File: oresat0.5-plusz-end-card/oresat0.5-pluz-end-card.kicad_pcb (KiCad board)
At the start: 4 copper layers, 99.8 x 94.6 mm, 44 parts, among them J1 J-SAMTEC-TFM-120-01-L-D-RA, J2 Harwin M55-7101242R, J3 Harwin M55-7101242R, J4 Harwin M55-7101242R, J5 Harwin M55-7101242R, J6 Conn_Coaxial

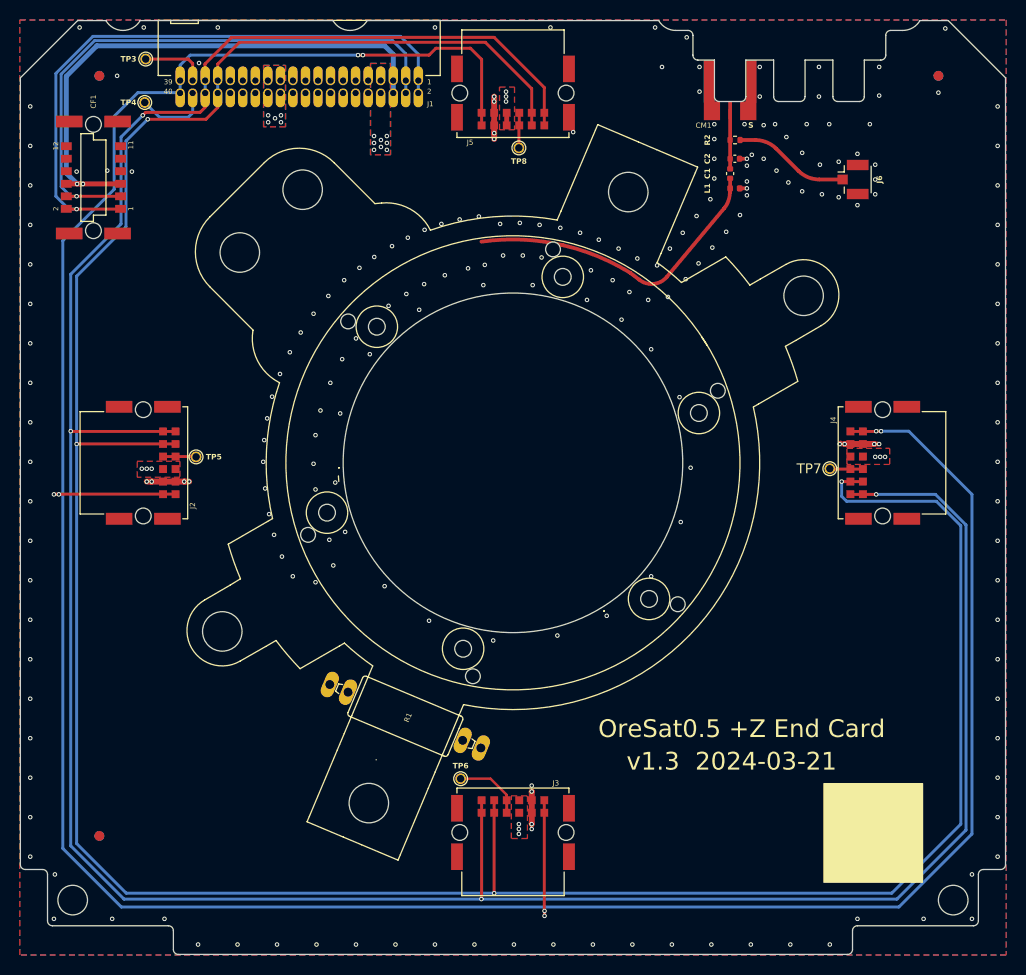
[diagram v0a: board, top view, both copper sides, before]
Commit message: Updated date, and unecessary and obsessive widening and smoothing of planes.
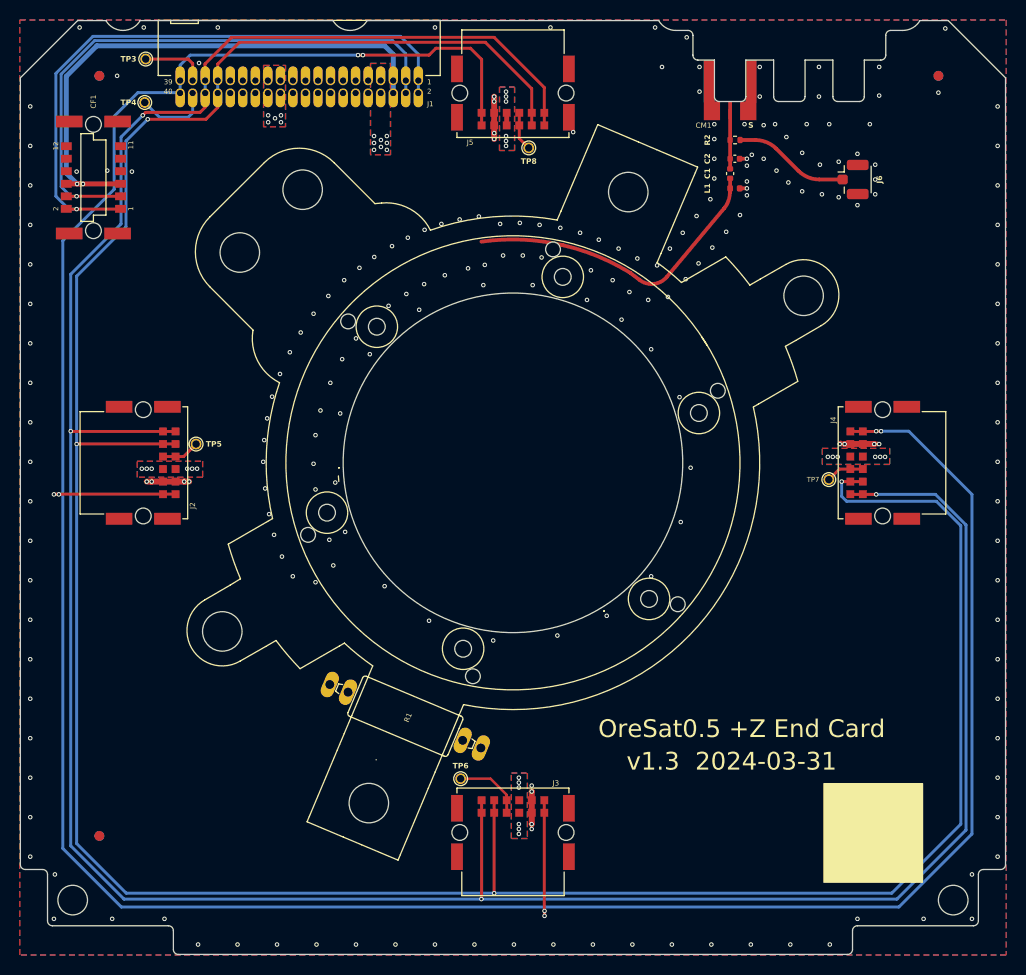
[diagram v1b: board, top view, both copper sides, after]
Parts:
- HW10, HW11, HW12, HW13, HW14, HW9: value Val** -> M2-Press-Fit-Nut
- moved TP5 1.30 mm to (116.4, 100.6)
- moved TP7 1.11 mm to (180.5, 104.2)
- moved TP8 1.00 mm to (150.1, 70.6)
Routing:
- net /-Y_AUX: track 3.66 -> 4.30 mm
- net /+Y_AUX: track 3.37 -> 3.89 mm
- net VBUS: vias 17 -> 29
- removed copper zone on In1.Cu, net /HELICAL-DEPLOY
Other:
- board text added: "v1.3 2024-03-31"
- board text removed: "v1.3 2024-03-21"

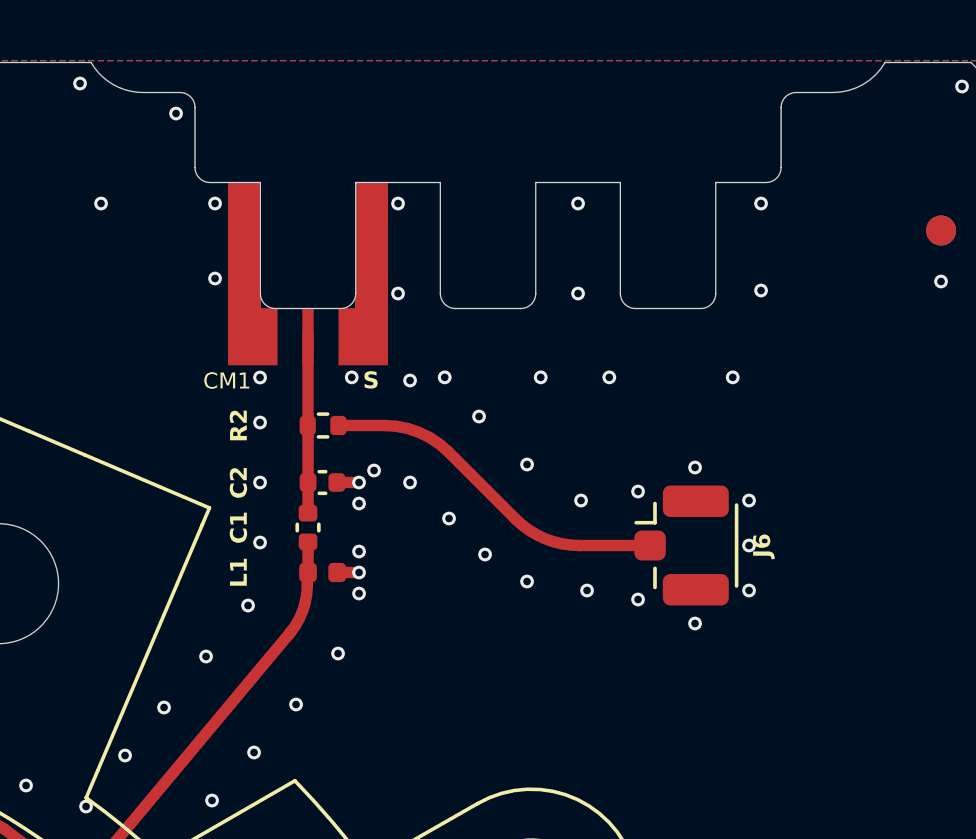
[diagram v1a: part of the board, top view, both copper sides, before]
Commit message: Updated helical matching network components and values
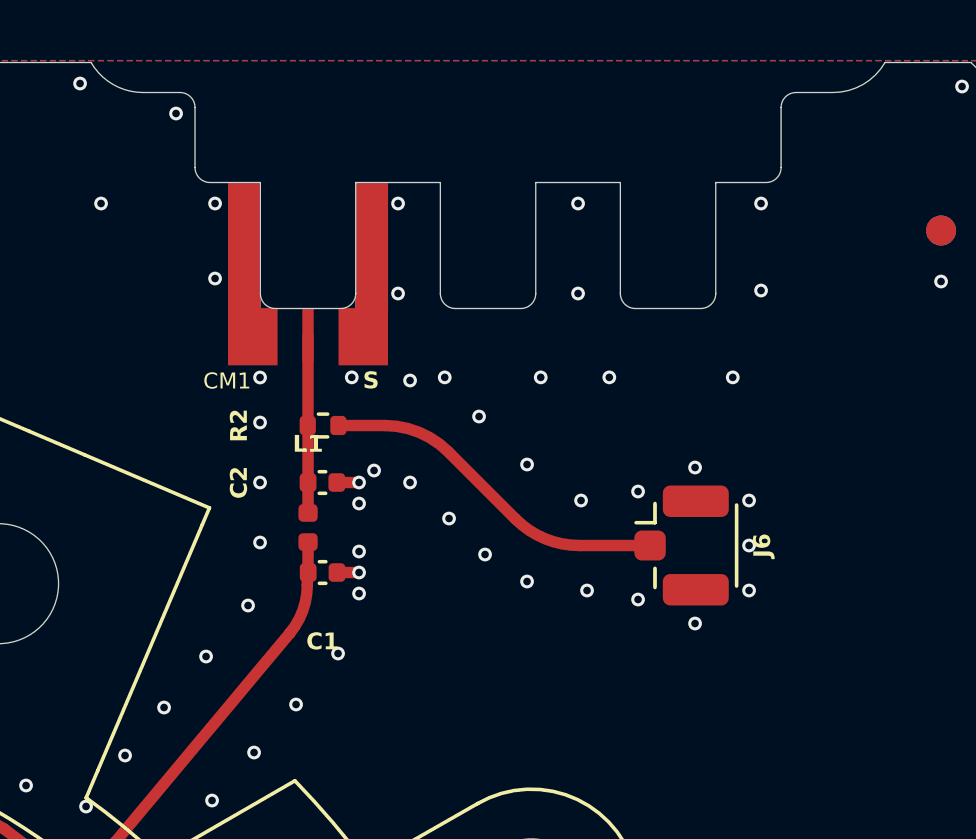
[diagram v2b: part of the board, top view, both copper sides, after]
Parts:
- C1: value C -> 1.0 pF
- C2: value NP -> 0.9 pF
- L1: value L -> 4.2 pF
- moved C1 1.58 mm to (171.0, 74.7), turned to 0 degrees
- moved L1 1.58 mm to (170.5, 73.2), turned to -90 degrees
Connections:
- C1 pad 1: /S_BAND -> /S_BAND_FEED
- C1 pad 2: /S_BAND_FEED -> GND
- L1 pad 1: /S_BAND_FEED -> /S_BAND
- L1 pad 2: GND -> /S_BAND_FEED
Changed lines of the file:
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@@
 			)
 		)
-		(property "Value" "NP"
+		(property "Value" "0.9 pF"
 			(at 0 1.16 0)
 			(layer "F.Fab")
@@
 		(fp_arc
 			(start 17.73205 -43.8)
-			(mid 18.085606 -43.653542)
+			(mid 18.085571 -43.653536)
 			(end 18.23205 -43.3)
 			(stroke
@@
 		(fp_arc
 			(start 18.73205 -40.8)
-			(mid 18.378494 -40.946458)
+			(mid 18.378529 -40.946464)
 			(end 18.23205 -41.3)
 			(stroke
@@
 		(fp_arc
 			(start 37.76795 -43.3)
-			(mid 37.9144 -43.653536)
+			(mid 37.914394 -43.653571)
 			(end 38.26795 -43.8)
 			(stroke
@@
 		(fp_arc
 			(start 37.76795 -41.3)
-			(mid 37.6215 -40.946464)
+			(mid 37.621506 -40.946429)
 			(end 37.26795 -40.8)
 			(stroke
@@
 		(fp_arc
 			(start 17.73205 -43.8)
-			(mid 18.085606 -43.653542)
+			(mid 18.085571 -43.653536)
 			(end 18.23205 -43.3)
 			(stroke
@@
 		(fp_arc
 			(start 18.73205 -40.8)
-			(mid 18.378494 -40.946458)
+			(mid 18.378529 -40.946464)
 			(end 18.23205 -41.3)
 			(stroke
@@
 		(fp_arc
 			(start 37.76795 -43.3)
-			(mid 37.9144 -43.653536)
+			(mid 37.914394 -43.653571)
 			(end 38.26795 -43.8)
 			(stroke
@@
 		(fp_arc
 			(start 37.76795 -41.3)
-			(mid 37.6215 -40.946464)
+			(mid 37.621506 -40.946429)
 			(end 37.26795 -40.8)
 			(stroke
@@
 	(footprint "Inductor_SMD:L_0402_1005Metric"
 		(layer "F.Cu")
-		(at 170.985 74.7)
+		(at 170.5 73.2 -90)
 		(descr "Inductor SMD 0402 (1005 Metric), square (rectangular) end terminal, IPC_7351 nominal, (Body size source: http://www.tortai-tech.com/upload/download/2011102023233369053.pdf), generated with kicad-footprint-generator")
 		(tags "inductor")
 		(property "Reference" "L1"
-			(at -2.785 0 90)
+			(at -2.785 0 180)
 			(layer "F.SilkS")
 			(effects
@@
 			)
 		)
-		(property "Value" "L"
-			(at -5.08 -0.508 0)
+		(property "Value" "4.2 pF"
+			(at -5.08 -0.508 90)
 			(layer "F.Fab")
 			(hide yes)
@@
 		)
 		(property "Footprint" "Inductor_SMD:L_0402_1005Metric"
-			(at 0 0 0)
+			(at 0 0 -90)
 			(unlocked yes)
 			(layer "F.Fab")
@@
 		)
 		(property "Datasheet" ""
-			(at 0 0 0)
+			(at 0 0 -90)
 			(unlocked yes)
 			(layer "F.Fab")
@@
 		)
 		(property "Description" ""
-			(at 0 0 0)
+			(at 0 0 -90)
 			(unlocked yes)
 			(layer "F.Fab")
@@
 		(attr smd)
 		(fp_line
-			(start -0.93 -0.47)
-			(end 0.93 -0.47)
+			(start -0.93 0.47)
+			(end -0.93 -0.47)
 			(stroke
 				(width 0.05)
@@
 		)
 		(fp_line
-			(start -0.93 0.47)
-			(end -0.93 -0.47)
+			(start 0.93 0.47)
+			(end -0.93 0.47)
 			(stroke
 				(width 0.05)
@@
 		)
 		(fp_line
-			(start 0.93 -0.47)
-			(end 0.93 0.47)
+			(start -0.93 -0.47)
+			(end 0.93 -0.47)
 			(stroke
 				(width 0.05)
@@
 		)
 		(fp_line
-			(start 0.93 0.47)
-			(end -0.93 0.47)
+			(start 0.93 -0.47)
+			(end 0.93 0.47)
 			(stroke
 				(width 0.05)
@@
 		)
 		(fp_line
-			(start -0.5 -0.25)
-			(end 0.5 -0.25)
+			(start -0.5 0.25)
+			(end -0.5 -0.25)
 			(stroke
 				(width 0.1)
@@
 		)
 		(fp_line
-			(start -0.5 0.25)
-			(end -0.5 -0.25)
+			(start 0.5 0.25)
+			(end -0.5 0.25)
 			(stroke
 				(width 0.1)
@@
 		)
 		(fp_line
-			(start 0.5 -0.25)
-			(end 0.5 0.25)
+			(start -0.5 -0.25)
+			(end 0.5 -0.25)
 			(stroke
 				(width 0.1)
@@
 		)
 		(fp_line
-			(start 0.5 0.25)
-			(end -0.5 0.25)
+			(start 0.5 -0.25)
+			(end 0.5 0.25)
 			(stroke
 				(width 0.1)
@@
 		)
 		(fp_text user "${REFERENCE}"
-			(at 0 0 0)
+			(at 0 0 90)
 			(layer "F.Fab")
 			(effects
@@
 		)
 		(pad "1" smd roundrect
-			(at -0.485 0)
+			(at -0.485 0 270)
 			(size 0.59 0.64)
 			(layers "F.Cu" "F.Paste" "F.Mask")
 			(roundrect_rratio 0.25)
-			(net 38 "/S_BAND_FEED")
+			(net 16 "/S_BAND")
 			(pinfunction "1")
 			(pintype "passive")
 		)
 		(pad "2" smd roundrect
-			(at 0.485 0)
+			(at 0.485 0 270)
 			(size 0.59 0.64)
 			(layers "F.Cu" "F.Paste" "F.Mask")
 			(roundrect_rratio 0.25)
-			(net 2 "GND")
+			(net 38 "/S_BAND_FEED")
 			(pinfunction "2")
 			(pintype "passive")
@@
 	(footprint "Capacitor_SMD:C_0402_1005Metric"
 		(layer "F.Cu")
-		(at 170.5 73.2 -90)
+		(at 170.985 74.7)
 		(descr "Capacitor SMD 0402 (1005 Metric), square (rectangular) end terminal, IPC_7351 nominal, (Body size source: IPC-SM-782 page 76, https://www.pcb-3d.com/wordpress/wp-content/uploads/ipc-sm-782a_amendment_1_and_2.pdf), generated with kicad-footprint-generator")
 		(tags "capacitor")
 		(property "Reference" "C1"
-			(at 0 2.3 90)
+			(at 0 2.3 360)
 			(layer "F.SilkS")
 			(effects
@@
 			)
 		)
-		(property "Value" "C"
-			(at -2.286 2.032 90)
+		(property "Value" "1.0 pF"
+			(at -2.286 2.032 360)
 			(layer "F.Fab")
 			(hide yes)
@@
 		)
 		(property "Footprint" "Capacitor_SMD:C_0402_1005Metric"
-			(at 0 0 -90)
+			(at 0 0 0)
 			(unlocked yes)
 			(layer "F.Fab")
@@
 		)
 		(property "Datasheet" ""
-			(at 0 0 -90)
+			(at 0 0 0)
 			(unlocked yes)
 			(layer "F.Fab")
@@
 		)
 		(property "Description" ""
-			(at 0 0 -90)
+			(at 0 0 0)
 			(unlocked yes)
 			(layer "F.Fab")
@@
 		(attr smd)
 		(fp_line
-			(start -0.107836 0.36)
-			(end 0.107836 0.36)
+			(start -0.107836 -0.36)
+			(end 0.107836 -0.36)
 			(stroke
 				(width 0.12)
@@
 		)
 		(fp_line
-			(start -0.107836 -0.36)
-			(end 0.107836 -0.36)
+			(start -0.107836 0.36)
+			(end 0.107836 0.36)
 			(stroke
 				(width 0.12)
@@
 		)
 		(fp_line
-			(start -0.91 0.46)
-			(end -0.91 -0.46)
+			(start -0.91 -0.46)
+			(end 0.91 -0.46)
 			(stroke
 				(width 0.05)
@@
 		)
 		(fp_line
-			(start 0.91 0.46)
-			(end -0.91 0.46)
+			(start -0.91 0.46)
+			(end -0.91 -0.46)
 			(stroke
 				(width 0.05)
@@
 		)
 		(fp_line
-			(start -0.91 -0.46)
-			(end 0.91 -0.46)
+			(start 0.91 -0.46)
+			(end 0.91 0.46)
 			(stroke
 				(width 0.05)
@@
 		)
 		(fp_line
-			(start 0.91 -0.46)
-			(end 0.91 0.46)
+			(start 0.91 0.46)
+			(end -0.91 0.46)
 			(stroke
 				(width 0.05)
@@
 		)
 		(fp_line
-			(start -0.5 0.25)
-			(end -0.5 -0.25)
+			(start -0.5 -0.25)
+			(end 0.5 -0.25)
 			(stroke
 				(width 0.1)
@@
 		)
 		(fp_line
-			(start 0.5 0.25)
-			(end -0.5 0.25)
+			(start -0.5 0.25)
+			(end -0.5 -0.25)
 			(stroke
 				(width 0.1)
@@
 		)
 		(fp_line
-			(start -0.5 -0.25)
-			(end 0.5 -0.25)
+			(start 0.5 -0.25)
+			(end 0.5 0.25)
 			(stroke
 				(width 0.1)
@@
 		)
 		(fp_line
-			(start 0.5 -0.25)
-			(end 0.5 0.25)
+			(start 0.5 0.25)
+			(end -0.5 0.25)
 			(stroke
 				(width 0.1)
@@
 		)
 		(pad "1" smd roundrect
-			(at -0.48 0 270)
+			(at -0.48 0)
 			(size 0.56 0.62)
 			(layers "F.Cu" "F.Paste" "F.Mask")
 			(roundrect_rratio 0.25)
-			(net 16 "/S_BAND")
+			(net 38 "/S_BAND_FEED")
 			(pintype "passive")
 		)
 		(pad "2" smd roundrect
-			(at 0.48 0 270)
+			(at 0.48 0)
 			(size 0.56 0.62)
 			(layers "F.Cu" "F.Paste" "F.Mask")
 			(roundrect_rratio 0.25)
-			(net 38 "/S_BAND_FEED")
+			(net 2 "GND")
 			(pintype "passive")
 		)

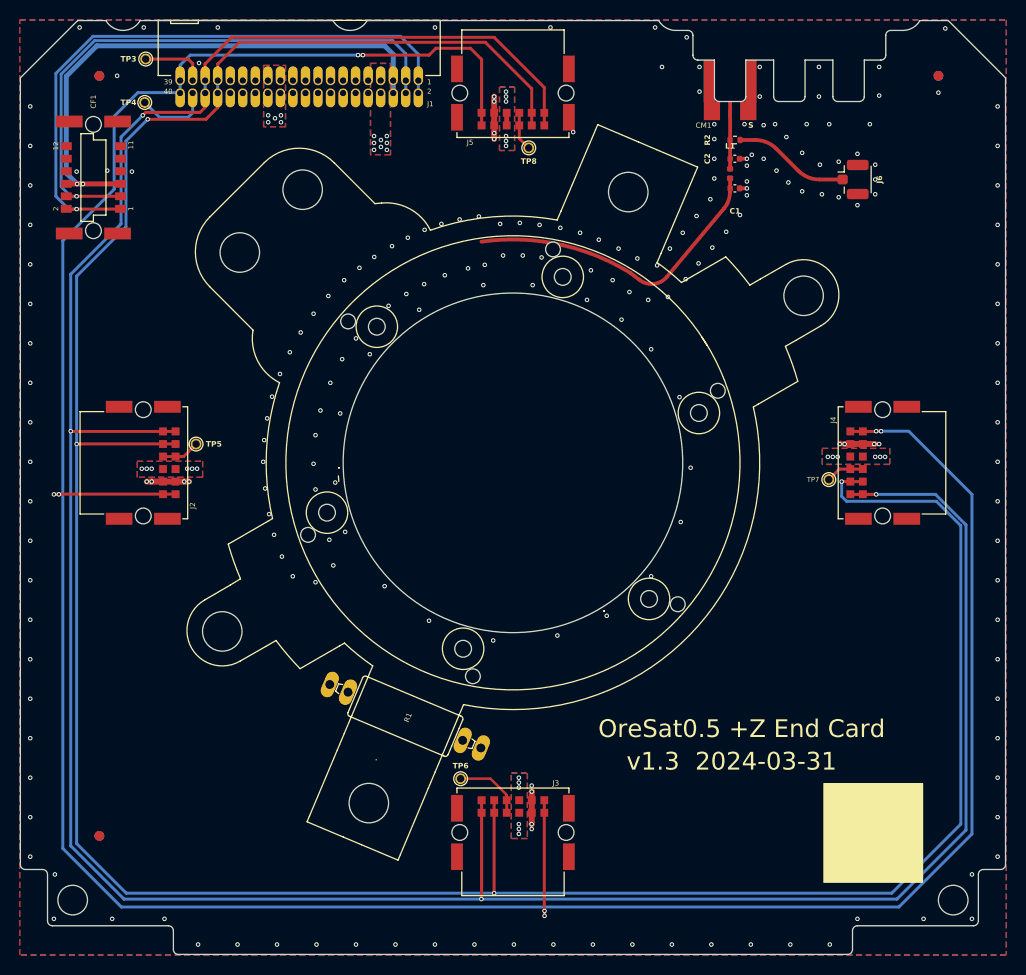
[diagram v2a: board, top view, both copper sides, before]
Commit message: Updated hole positions for single door deployer. TODO: fix weird net class errors that shouldn't exist.
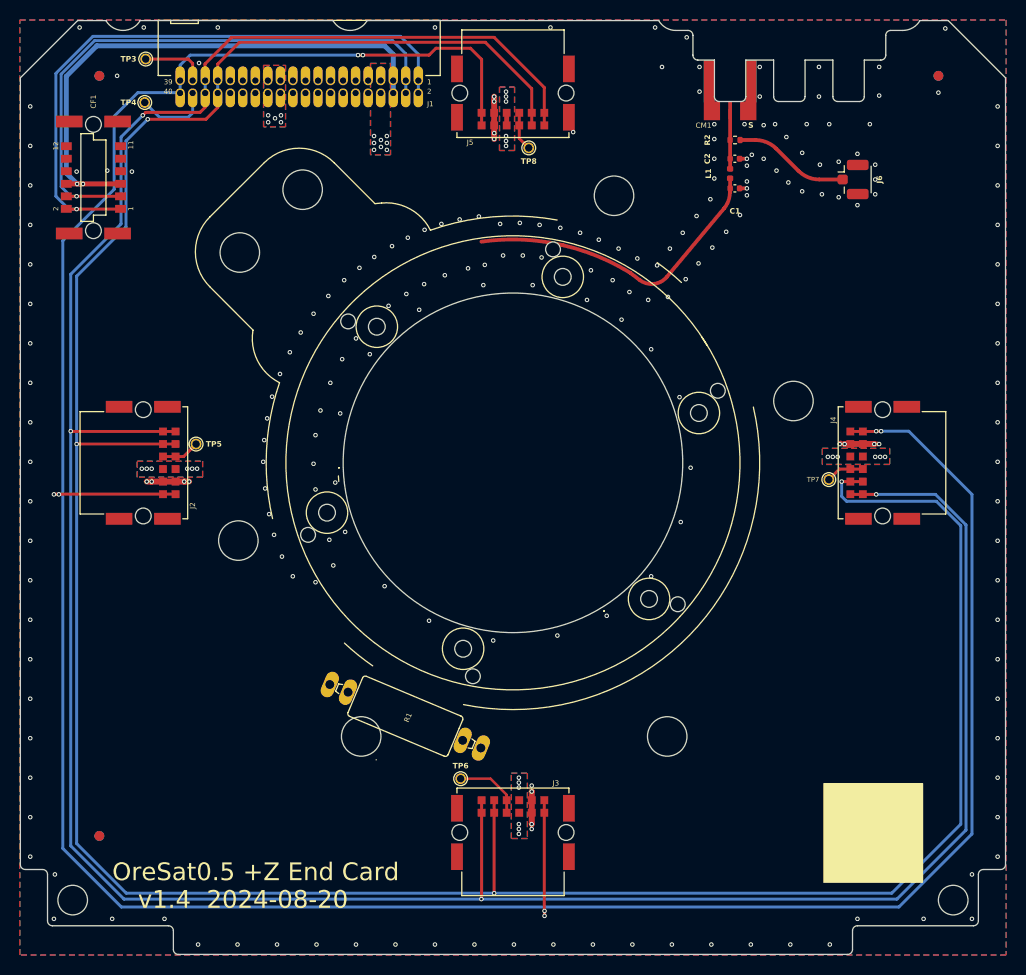
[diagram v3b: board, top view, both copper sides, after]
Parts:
- added HW4: M2-Press-Fit-Nut, oresat-misc:M2-Press-Fit-Nut, F.Cu at (164.1, 130.2)
- L1: value 4.2 pF -> 4.3 nH
- moved HW14 10.7 mm to (176.9, 96.2)
- moved HW10 9.35 mm to (120.7, 110.4)
- moved HW11 6.80 mm to (133.1, 130.2)
- moved HW13 1.49 mm to (158.7, 75.4)
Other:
- board text added: "v1.4 2024-08-20"
- board text removed: "v1.3 2024-03-31"

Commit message: changed resistor placement
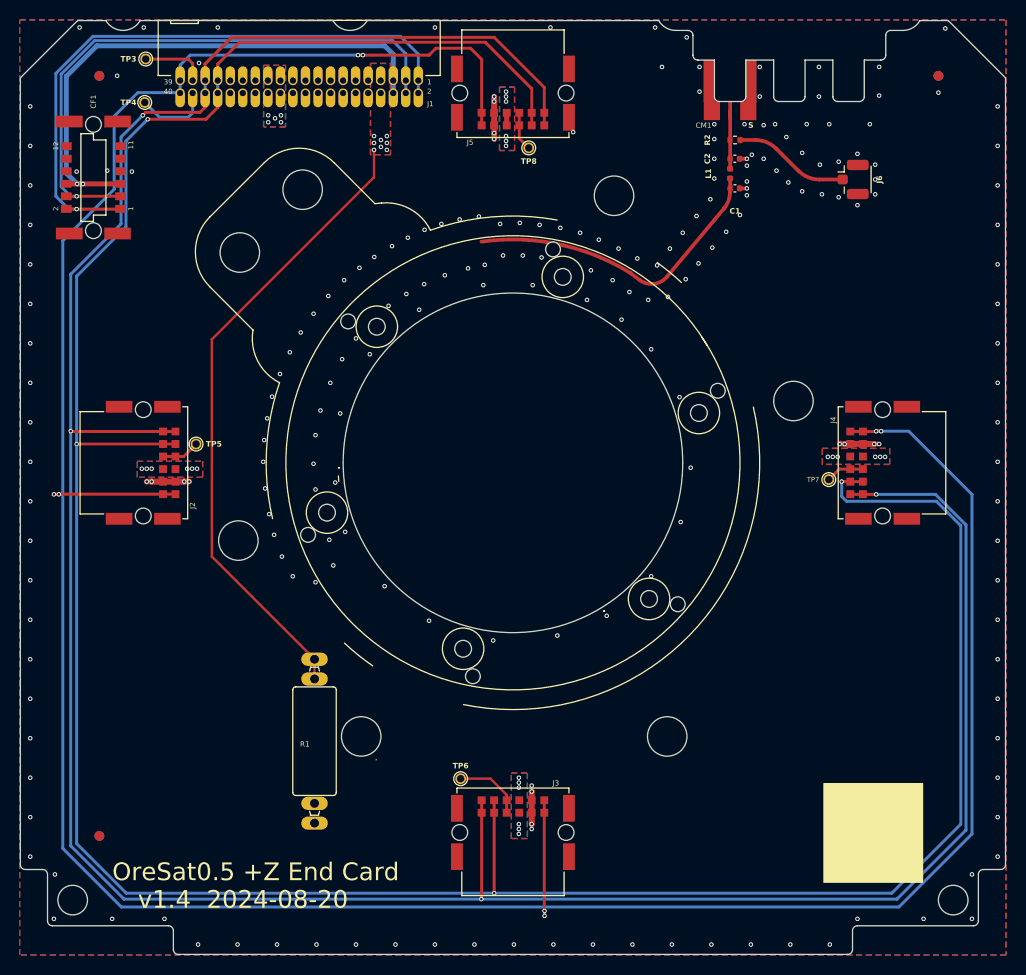
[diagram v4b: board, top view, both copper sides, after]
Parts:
- moved R1 9.54 mm to (128.4, 130.7), turned to 180 degrees
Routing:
- net /HELICAL-DEPLOY: track 0.00 -> 64.7 mm
